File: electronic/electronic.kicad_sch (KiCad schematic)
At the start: 67 parts, among them J1 M_BAT01, J10 BMP01, J11 MPU6050_01, J12 NEO_06_01, J13 CONN, J14 SSD1306_OLED, J2 M_SIG01, J3 M_SIG01, J4 M_BAT01, J5 M_SIG01, J6 M_BAT01, J7 M_SIG01, J8 M_BAT01, J9 DHT01, M1 A2212 KV2200, M2 A2212 KV2200, M3 A2212 KV2200, M4 A2212 KV2200, U1 30A ESC, U11 RT9193-33GB, U12 CAT24C256, U13 SSD1306, U14 ESP32-DevKitC, U2 30A ESC, U3 30A ESC, U4 30A ESC, U5 BMP280, U6 DHT22, U7 AP2112K-1.2, U8 NEO-6M-GPS, U9 MPU-6050

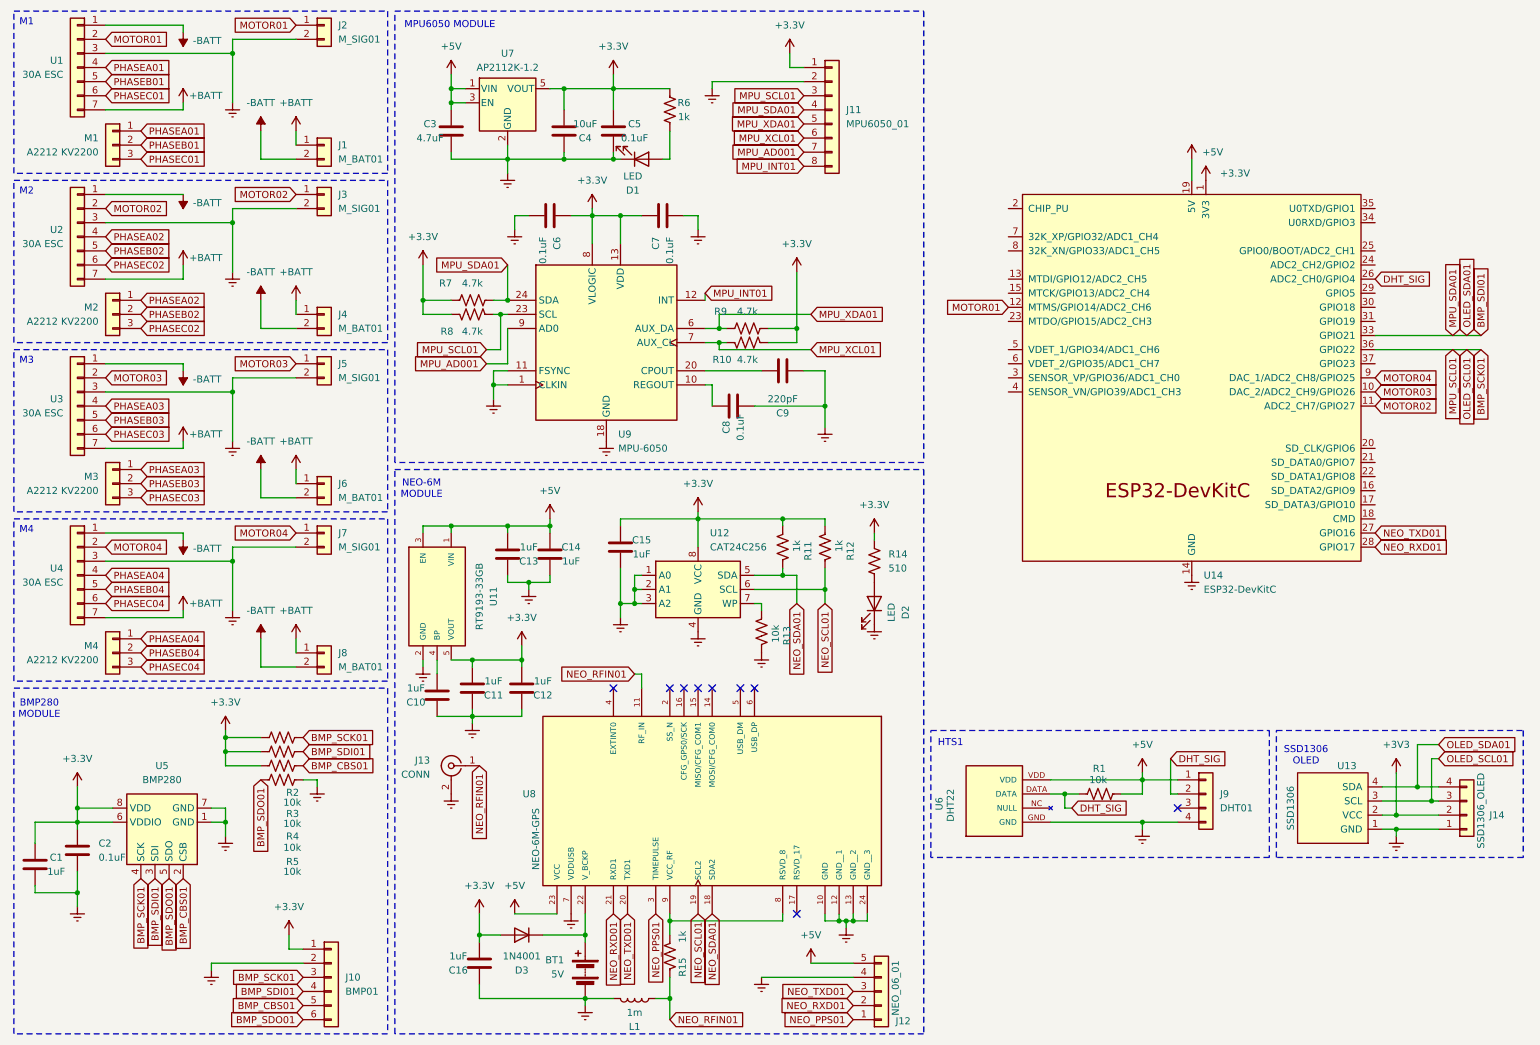
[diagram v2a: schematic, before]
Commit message: chore: ESP32 devkit changed of schematic
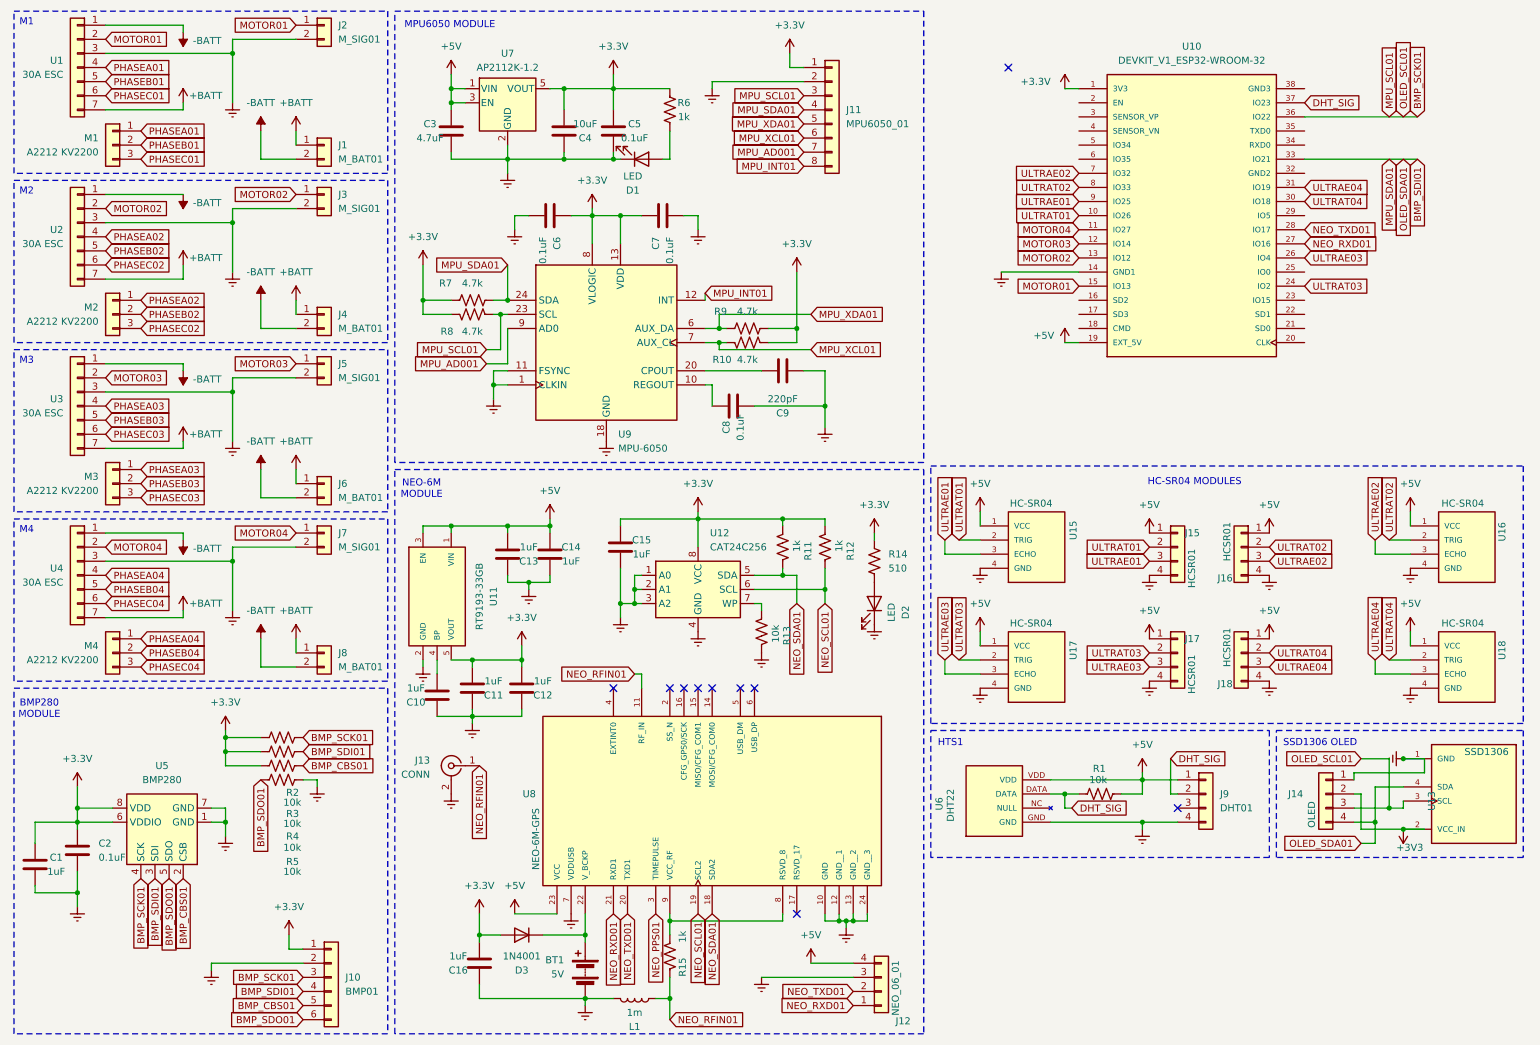
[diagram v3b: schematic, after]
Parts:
- removed U14: ESP32-DevKitC, RF_Module:ESP32-S2-WROVER, symbol PCM_Espressif:ESP32-DevKitC
- added J15, J16, J17, J18: HCSR01, Connector_PinHeader_2.54mm:PinHeader_1x04_P2.54mm_Vertical, symbol Connector_Generic:Conn_01x04
- added U10: DEVKIT_V1_ESP32-WROOM-32, custom:MODULE_DEVKIT_V1_ESP32-WROOM-32, symbol DEVKIT_V1_ESP32-WROOM-32:DEVKIT_V1_ESP32-WROOM-32
- added U15, U16, U17, U18: HC-SR04, HC-SR04:XCVR_HC-SR04, symbol HC-SR04:HC-SR04
- BT1, C10, C11, C12, C13, C14, C15, C16, C3, C4, C5, C6, C7, C8, C9, D1, D2, D3, J13, L1, R10, R11, R12, R13, R14, R15, R6, R7, R8, R9, U11, U12, U7, U8, U9: now left out of the parts list
- J1, J2, J3, J4, J5, J6, J7, J8: footprint (none) -> Connector_JST:JST_XH_B2B-XH-A_1x02_P2.50mm_Vertical
- J10: footprint (none) -> Connector_PinHeader_2.54mm:PinHeader_1x06_P2.54mm_Vertical
- J11: footprint (none) -> Connector_PinHeader_2.54mm:PinHeader_1x08_P2.54mm_Vertical
- J12: footprint (none) -> Connector_PinHeader_2.54mm:PinHeader_1x04_P2.54mm_Vertical; symbol Connector_Generic:Conn_01x05 -> Connector_Generic:Conn_01x04
- J14: value SSD1306_OLED -> OLED; footprint (none) -> Connector_PinHeader_2.54mm:PinHeader_1x04_P2.54mm_Vertical
- J9: footprint (none) -> Connector_PinHeader_2.54mm:PinHeader_1x04_P2.54mm_Vertical
- R1: footprint (none) -> Resistor_THT:R_Axial_DIN0207_L6.3mm_D2.5mm_P10.16mm_Horizontal
- U13: footprint (none) -> custom:MODULE_DM-OLED096-636; symbol custom:SSD1306 -> custom:DM-OLED096-636; Availability (none) -> Not in stock; Check_prices (none) -> https://www.snapeda.com/parts/DM-OLED096-636/Display+Module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; Description_1 (none) -> 0.96” 128 X 64 MONOCHROME GRAPHIC OLED DISPLAY MODULE - I2C; MANUFACTURER (none) -> Displaymodule; MAXIMUM_PACKAGE_HEIGHT (none) -> 11.3 mm; MF (none) -> Display Module; MP (none) -> DM-OLED096-636; PARTREV (none) -> 2018-09-10; Package (none) -> Package; Price (none) -> None; STANDARD (none) -> Manufacturer Recommendations; SnapEDA_Link (none) -> https://www.snapeda.com/parts/DM-OLED096-636/Display+Module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
- U6: footprint DHT22:DHT22 -> custom:DHT22
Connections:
- net +3.3V: now also U10.1 (3V3)
- net +5V: now also J12.4 (Pin_4), J15.1 (Pin_1), J16.1 (Pin_1), J17.1 (Pin_1), J18.1 (Pin_1), U10.19 (EXT_5V), U15.1 (VCC), U16.1 (VCC), U17.1 (VCC), U18.1 (VCC); no longer J12.5 (Pin_5)
- net BMP_SCK01: now also U10.36 (IO22)
- net BMP_SDI01: now also U10.33 (IO21)
- net DHT_SIG: now also U10.37 (IO23)
- net Earth: now also J12.3 (Pin_3), J15.4 (Pin_4), J16.4 (Pin_4), J17.4 (Pin_4), J18.4 (Pin_4), U10.14 (GND1), U15.4 (GND), U16.4 (GND), U17.4 (GND), U18.4 (GND); no longer J12.4 (Pin_4)
- net MOTOR01: now also U10.15 (IO13)
- net MOTOR02: now also U10.13 (IO12)
- net MOTOR03: now also U10.12 (IO14)
- net MOTOR04: now also U10.11 (IO27)
- net NEO_PPS01: no longer J12.1 (Pin_1)
- net NEO_RXD01: now also J12.1 (Pin_1), U10.27 (IO16); no longer J12.2 (Pin_2)
- net NEO_TXD01: now also J12.2 (Pin_2), U10.28 (IO17); no longer J12.3 (Pin_3)
- new net ULTRAE01: J15.3 (Pin_3), U10.9 (IO25), U15.3 (ECHO)
- new net ULTRAE02: J16.3 (Pin_3), U10.7 (IO32), U16.3 (ECHO)
- new net ULTRAE03: J17.3 (Pin_3), U10.26 (IO4), U17.3 (ECHO)
- new net ULTRAE04: J18.3 (Pin_3), U10.31 (IO19), U18.3 (ECHO)
- new net ULTRAT01: J15.2 (Pin_2), U10.10 (IO26), U15.2 (TRIG)
- new net ULTRAT02: J16.2 (Pin_2), U10.8 (IO33), U16.2 (TRIG)
- new net ULTRAT03: J17.2 (Pin_2), U10.24 (IO2), U17.2 (TRIG)
- new net ULTRAT04: J18.2 (Pin_2), U10.30 (IO18), U18.2 (TRIG)
- no-connect marks 9 -> 10
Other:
- note added: "HC-SR04 MODULES"
- moved on the sheet: J14

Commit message: chore: PCB design added to the project
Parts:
- added C17: 220u, Capacitor_THT:C_Radial_D8.0mm_H11.5mm_P3.50mm, symbol Device:C_Polarized_US
- added J19: BAT, custom:DG301-5.0-2P-1X, symbol Connector:Screw_Terminal_01x02
- added U14: L7805, Package_TO_SOT_SMD:TO-252-2, symbol Regulator_Linear:L7805
- J16: value HCSR01 -> HCSR02
- J17: value HCSR01 -> HCSR03
- J18: value HCSR01 -> HCSR04
- J3: value M_SIG01 -> M_SIG02
- J4: value M_BAT01 -> M_BAT02
- J5: value M_SIG01 -> M_SIG03
- J6: value M_BAT01 -> M_BAT03
- J7: value M_SIG01 -> M_SIG04
- J8: value M_BAT01 -> M_BAT04
- J9: footprint Connector_PinHeader_2.54mm:PinHeader_1x04_P2.54mm_Vertical -> custom:DHT22
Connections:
- net +5V: now also C17.1, U14.3 (OUT)
- net +BATT: now also J19.1 (Pin_1), U14.1 (IN)
- net -BATT: now also J19.2 (Pin_2)
- net Earth: now also U10.32 (GND2), U10.38 (GND3), C17.2, U14.2 (GND)
- net MOTOR01: now also U10.11 (IO27); no longer U10.15 (IO13)
- net MOTOR02: now also U10.12 (IO14); no longer U10.13 (IO12)
- net MOTOR03: now also U10.15 (IO13); no longer U10.12 (IO14)
- net MOTOR04: now also U10.13 (IO12); no longer U10.11 (IO27)
- net ULTRAE02: now also U10.8 (IO33); no longer U10.7 (IO32)
- net ULTRAT02: now also U10.7 (IO32); no longer U10.8 (IO33)
- no-connect marks 10 -> 25
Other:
- note added: "POWER"
- moved on the sheet: U10

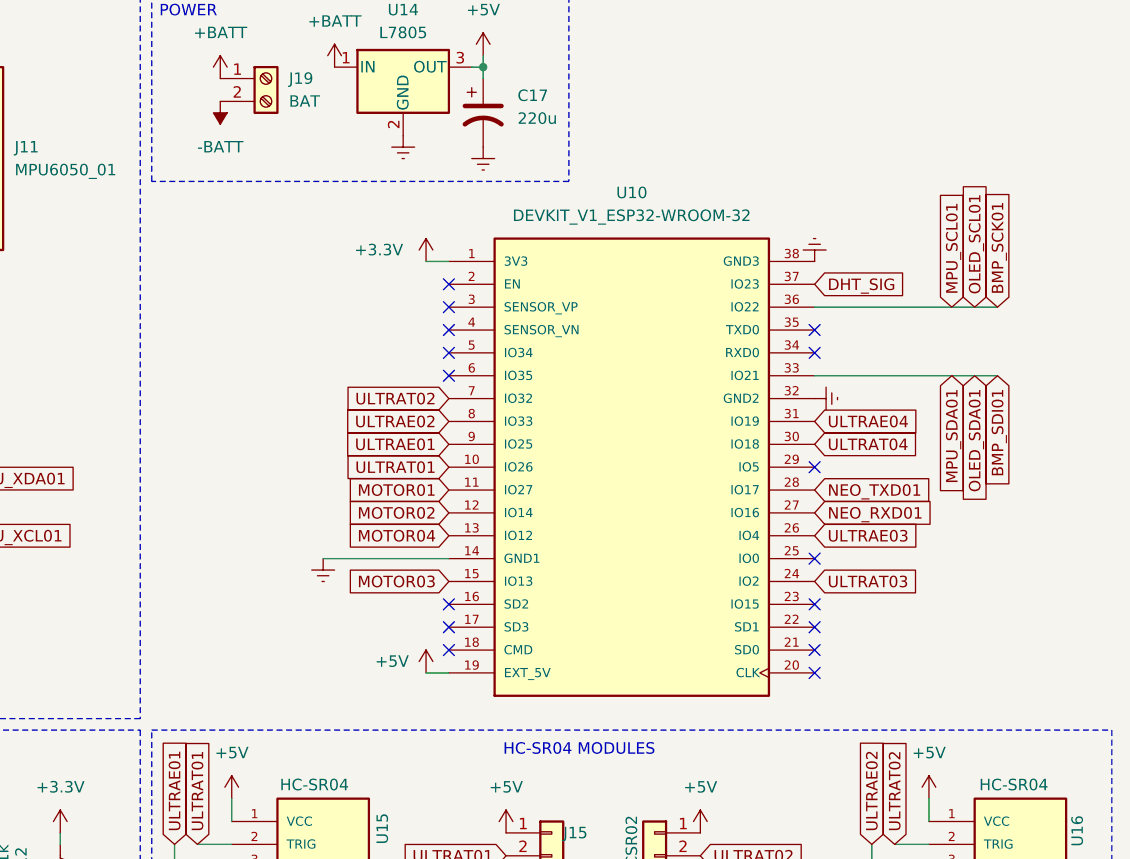
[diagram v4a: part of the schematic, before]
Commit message: refactor (electronic): update PCB design
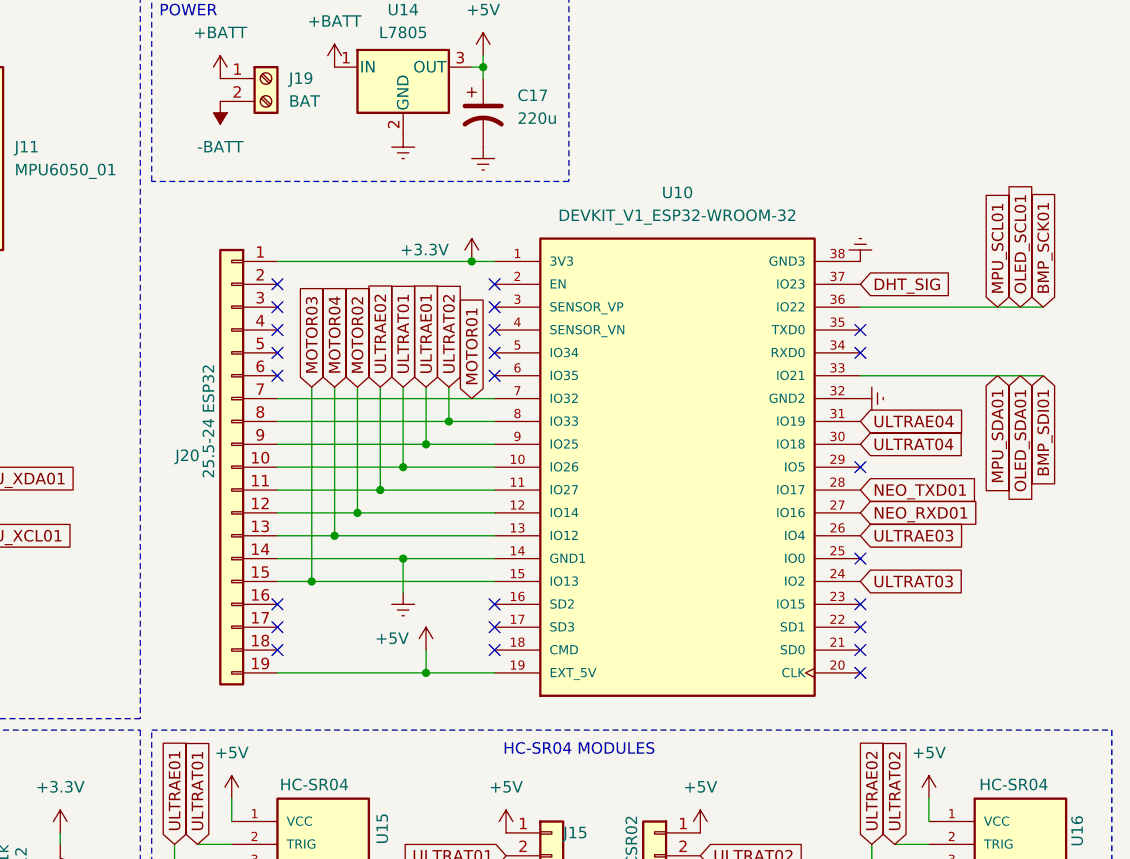
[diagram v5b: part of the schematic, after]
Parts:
- added J20: 25.5-24 ESP32, Connector_PinSocket_2.54mm:PinSocket_1x19_P2.54mm_Vertical, symbol Connector_Generic:Conn_01x19
- J9: now left out of the parts list
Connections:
- net +3.3V: now also J20.1 (Pin_1)
- net +5V: now also J20.19 (Pin_19)
- net Earth: now also J20.14 (Pin_14)
- net MOTOR01: now also U10.7 (IO32), J20.7 (Pin_7); no longer U10.11 (IO27)
- net MOTOR02: now also J20.12 (Pin_12)
- net MOTOR03: now also J20.15 (Pin_15)
- net MOTOR04: now also J20.13 (Pin_13)
- net ULTRAE01: now also J20.9 (Pin_9)
- net ULTRAE02: now also U10.11 (IO27), J20.11 (Pin_11); no longer U10.8 (IO33)
- net ULTRAT01: now also J20.10 (Pin_10)
- net ULTRAT02: now also U10.8 (IO33), J20.8 (Pin_8); no longer U10.7 (IO32)
- no-connect marks 25 -> 33
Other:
- moved on the sheet: U10
